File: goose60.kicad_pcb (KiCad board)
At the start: 2 copper layers, 285 x 94.6 mm, 190 parts, among them J1 Debugger, J2 USART, J3 SPI, P1 USB_C_Plug_USB2.0, SW1 SW_Push, SW10 SW_Push, SW11 SW_Push, SW14 SW_Push, SW15 SW_Push, SW16 SW_Push, SW18 SW_Push, SW2 SW_Push, SW20 SW_Push, SW21 SW_Push, SW22 SW_Push, SW23 SW_Push, SW24 SW_Push, SW25 SW_Push, SW26 SW_Push, SW27 SW_Push, SW28 SW_Push, SW29 SW_Push, SW3 SW_Push, SW30 SW_Push, SW31 SW_Push, SW32 SW_Push, SW35 SW_Push, SW36 SW_Push, SW37 SW_Push, SW38 SW_Push, SW39 SW_Push, SW40 SW_Push, SW41 SW_Push, SW42 SW_Push, SW43 SW_Push, SW44 SW_Push, SW45 SW_Push, SW46 SW_Push, SW47 SW_Push, SW48 SW_Push, SW49 SW_Push, SW5 SW_Push, SW50 SW_Push, SW51 SW_Push, SW52 SW_Push, SW53 SW_Push, SW54 SW_Push, SW56 SW_Push, SW58 SW_Push, SW59 SW_Push, SW60 SW_Push, SW61 SW_Push, SW62 SW_Push, SW65 SW_Push, SW66 SW_Push, SW67 SW_Push, SW68 SW_Push, SW69 SW_Push, SW7 SW_Push, SW71 SW_Push, SW73 SW_Push, SW74 SW_Push, SW75 SW_Push, SW76 SW_Push, SW78 SW_Push, SW79 SW_Push, SW80 SW_Push, SW82 SW_Push, SW84 SW_Push, SW86 SW_Push, SW9 SW_Push, U1 STM32F103CBTx, U2 LM317_SOT-223, X1 Crystal_GND24

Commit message: change pin default and try layout
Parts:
- removed ? (x4): , 
- removed HOLE: VAL**, hole:PKRH
- removed HOLE: VAL**, hole:PKRHSL
- removed P1: USB_C_Plug_USB2.0, Connector_USB:USB_C_Receptacle_HRO_TYPE-C-31-M-12
- removed R10, R9: 20, Resistor_SMD:R_0603_1608Metric
- removed R11: 1.5K, Resistor_SMD:R_0603_1608Metric
- added J4: USB_C_Receptacle_USB2.0, Connector_USB:USB_C_Receptacle_HRO_TYPE-C-31-M-12, B.Cu at (80.7, 66.5)
- added U3: USBLC6-2SC6, Package_TO_SOT_SMD:SOT-23-6, B.Cu at (94.0, 86.8)
- H2, H3, H5, H6: footprint MountingHole:MountingHole_3.2mm_M3_Pad -> MountingHole:MountingHole_3.2mm_M3_Pad_TopOnly
- H4: footprint MountingHole:MountingHole_3.2mm_M3 -> MountingHole:MountingHole_3.2mm_M3_Pad_TopOnly
- J2, J3: moved to B.Cu
- R25: value 0 -> 5.1K
- moved H1 170.5 mm to (87.7, 93.1)
- moved H4 115.1 mm to (253.0, 150.4)
- moved H3 106.1 mm to (322.6, 93.1)
- moved H2 90.6 mm to (190.7, 112.2)
- moved C9 38.5 mm to (131.0, 91.9)
- moved R5 38.5 mm to (129.1, 91.9)
- moved R6 38.5 mm to (127.2, 91.9)
- moved C10 38.3 mm to (140.0, 86.3)
- moved C11 38.2 mm to (124.7, 87.0)
- moved R4 38.2 mm to (125.3, 89.7)
- moved U2 38.2 mm to (133.1, 86.3)
- moved C8 38.2 mm to (126.9, 84.5)
- moved D69 38.2 mm to (124.8, 84.5)
- moved D70 38.2 mm to (127.3, 88.3)
- moved D6 20.8 mm to (82.5, 157.9), turned to 0 degrees
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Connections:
- J3 pad 2: SCK -> MOSI
- J3 pad 3: MOSI -> MISO
- J3 pad 4: MISO -> SCK
- R22 pad 2: PA8 -> PA4
- SW32 pad 2: col6 -> col7
- U1 pad 14: CAPS_LED -> PA4
- U1 pad 18: row2 -> col14
- U1 pad 20: col8 -> col13
- U1 pad 21: col9 -> col12
- U1 pad 22: col10 -> col11
- U1 pad 25: col11 -> col3
- U1 pad 26: col12 -> col2
- U1 pad 27: col13 -> col1
- U1 pad 28: col14 -> col4
- U1 pad 29: PA8 -> CAPS_LED
- U1 pad 39: col1 -> col5
- U1 pad 40: col2 -> col6
- U1 pad 41: col3 -> col7
- U1 pad 42: col4 -> col8
- U1 pad 43: col5 -> col9
- U1 pad 45: col6 -> row2
- U1 pad 46: col7 -> col10
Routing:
- net row2: track 0.00 -> 370.8 mm, vias 0 -> 16
- net row1: track 0.00 -> 304.4 mm, vias 0 -> 2
- net row4: track 0.00 -> 277.4 mm, vias 0 -> 13
- net row3: track 0.00 -> 269.3 mm, vias 0 -> 13
- net col13: track 0.00 -> 263.6 mm, vias 0 -> 3
- net row5: track 0.00 -> 259.0 mm
- net col10: track 0.00 -> 176.2 mm, vias 0 -> 2
- net col9: track 0.00 -> 160.0 mm, vias 0 -> 2
- net col1: track 0.00 -> 157.3 mm, vias 0 -> 2
- net col8: track 0.00 -> 142.6 mm, vias 0 -> 2
- net col7: track 0.00 -> 139.4 mm, vias 0 -> 2
- net col2: track 0.00 -> 137.9 mm, vias 0 -> 4
- net col14: track 0.00 -> 135.5 mm, vias 0 -> 3
- net col3: track 0.00 -> 118.9 mm, vias 0 -> 2
- net +3.3V: track 0.00 -> 117.1 mm
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
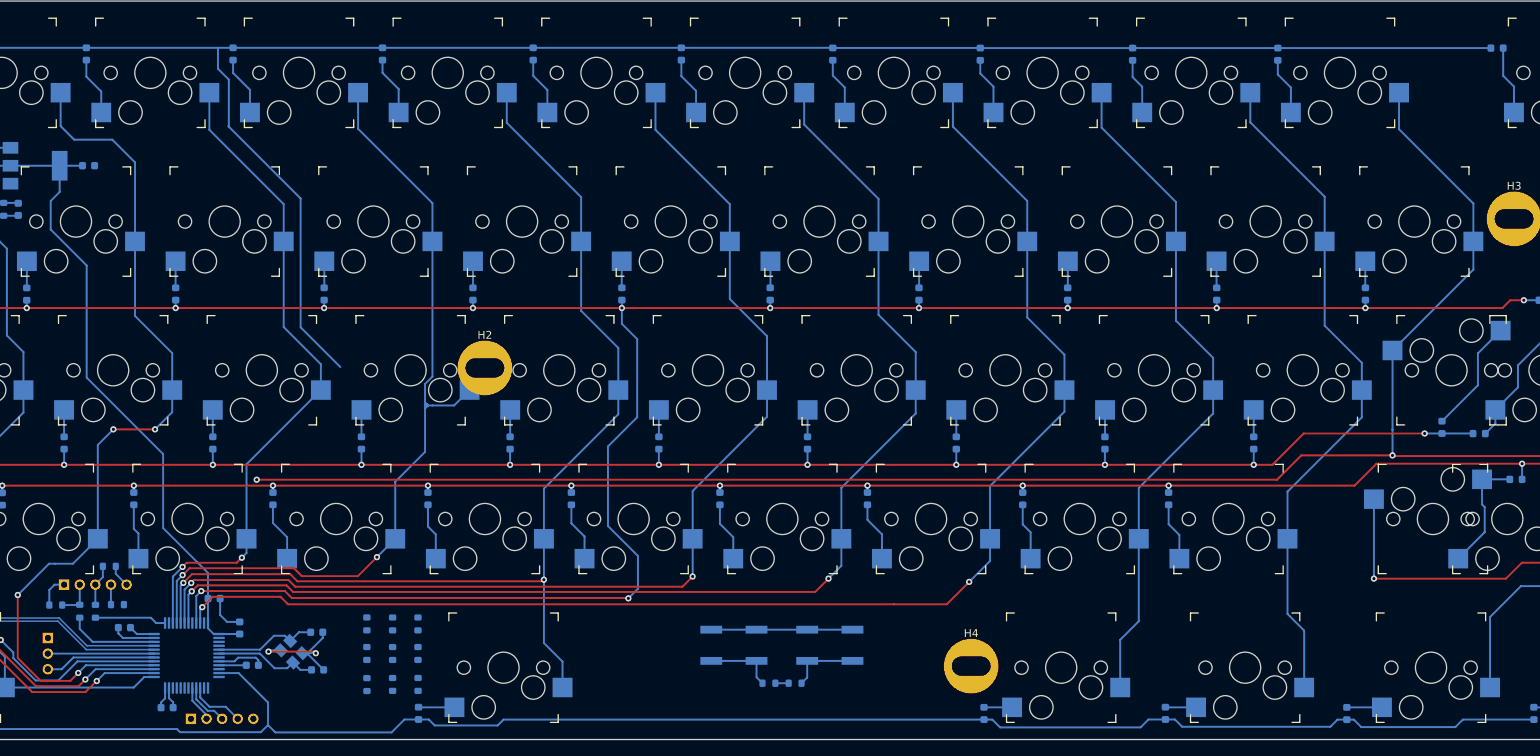
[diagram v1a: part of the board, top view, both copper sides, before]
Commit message: update pcb layout and pin defined
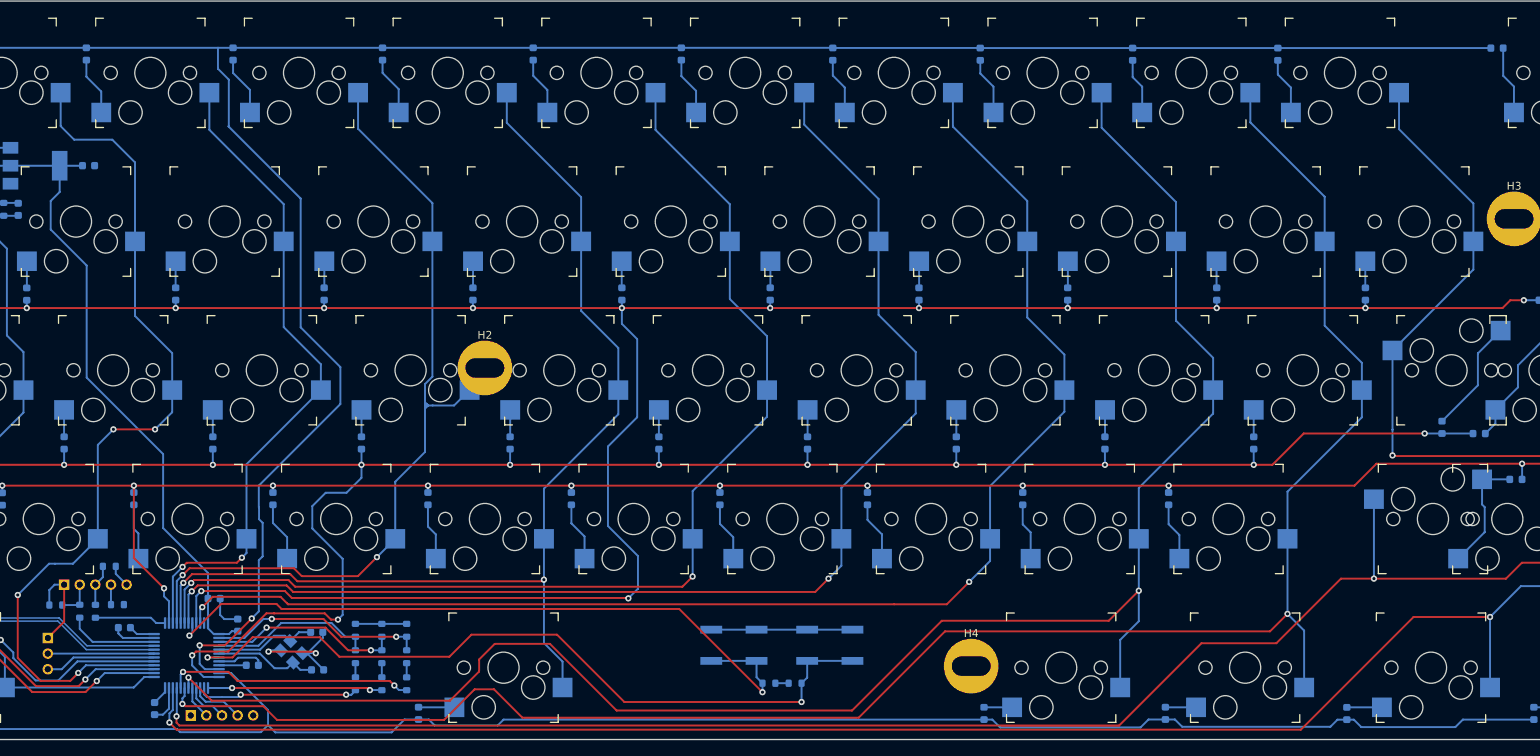
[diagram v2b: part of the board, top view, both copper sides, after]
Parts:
- moved R15 1.67 mm to (174.2, 145.8)
- moved R19 1.66 mm to (180.7, 145.8)
- moved C5 1.60 mm to (148.4, 155.8), turned to -90 degrees
- moved R17 1.60 mm to (177.5, 145.8)
- moved R16 1.52 mm to (174.2, 149.2)
- moved R20 1.51 mm to (180.7, 149.2)
- moved R23 1.47 mm to (174.2, 152.7)
- moved R21 1.46 mm to (180.7, 152.7)
- moved R18 1.44 mm to (177.5, 149.2)
- moved R22 1.38 mm to (177.5, 152.7)
- moved C3 0.44 mm to (159.1, 145.2)
- moved J3 0.43 mm to (153.1, 156.7)
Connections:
- R21 pad 2: PA0 -> PB2
- R22 pad 2: PA4 -> PA3
- R23 pad 2: PA15 -> PA4
- U1 pad 10: PA0 -> row1
- U1 pad 12: row4 -> row3
- U1 pad 13: row3 -> PA3
- U1 pad 18: col14 -> col11
- U1 pad 19: row1 -> col12
- U1 pad 20: col13 -> PB2
- U1 pad 21: col12 -> col14
- U1 pad 22: col11 -> col13
- U1 pad 38: PA15 -> row4
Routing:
- net col14: track 135.5 -> 301.4 mm, vias 3 -> 4
- net col12: track 86.9 -> 240.2 mm, vias 0 -> 2
- net col11: track 87.0 -> 225.2 mm, vias 0 -> 2
- net RESET: track 8.96 -> 95.8 mm, vias 0 -> 2
- net BOOT0: track 8.98 -> 91.7 mm, vias 0 -> 2
- net row3: track 269.3 -> 321.7 mm, vias 13 -> 15
- net row1: track 304.4 -> 355.0 mm, vias 2 -> 4
- net col13: track 263.6 -> 297.0 mm, vias 3 -> 4
- net PB2: track 0.00 -> 31.8 mm, vias 0 -> 2
- net PC13: track 0.00 -> 27.7 mm, vias 0 -> 2
- net PC14: track 0.00 -> 24.6 mm, vias 0 -> 2
- net PA3: track 0.00 -> 22.3 mm, vias 0 -> 2
- net PC15: track 0.00 -> 21.2 mm
- net PA4: track 0.00 -> 20.8 mm, vias 0 -> 2
- net row4: track 277.4 -> 296.9 mm, vias 13 -> 14
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
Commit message: add usb enable pin
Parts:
- removed R23: 10K, Resistor_SMD:R_0603_1608Metric
- added H7: MountingHole_Pad, NetTie:NetTie-2_SMD_Pad0.5mm, B.Cu at (82.1, 73.0)
- added H8: MountingHole_Pad, NetTie:NetTie-2_SMD_Pad0.5mm, B.Cu at (79.3, 73.0)
- added Q1: Q_NMOS_GSD, Package_TO_SOT_SMD:SOT-23, B.Cu at (110.0, 83.9)
- added R10: 22, Resistor_SMD:R_0603_1608Metric, B.Cu at (101.8, 85.9)
- added R11: 1.5K, Resistor_SMD:R_0603_1608Metric, B.Cu at (101.8, 83.9)
- added R26: 10K, Resistor_SMD:R_0603_1608Metric, B.Cu at (114.7, 84.8)
- added R9: 22, Resistor_SMD:R_0603_1608Metric, B.Cu at (101.8, 87.8)
- moved D22 1.40 mm to (130.3, 129.1)
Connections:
- J4 pad A8: unconnected-(J4-PadA8) -> Net-(J4-PadA8)
- J4 pad B8: unconnected-(J4-PadB8) -> Net-(J4-PadB8)
- U1 pad 14: PA4 -> USB_EN
- U3 pad 4: USB_D+ -> Net-(U3-Pad4)
- U3 pad 6: USB_D- -> Net-(U3-Pad6)
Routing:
- net USB_EN: track 0.00 -> 108.9 mm, vias 0 -> 4
- net +3.3V: track 123.3 -> 189.7 mm
- net PA4: track 20.8 -> 0.00 mm, vias 2 -> 0
- net VIN: track 67.6 -> 86.1 mm
- net Net-(U3-Pad4): track 0.00 -> 7.79 mm
- net Net-(R11-Pad2): track 0.00 -> 6.44 mm
- net Net-(U3-Pad6): track 0.00 -> 5.80 mm
- net col3: track 118.9 -> 113.8 mm, vias 2 -> 4
- net USB_D-: track 98.9 -> 94.0 mm
- net USB_D+: track 98.9 -> 93.9 mm
- net BOOT0: track 91.7 -> 88.7 mm
- net Net-(R26-Pad1): track 0.00 -> 2.95 mm
- net Net-(C9-Pad1): track 7.97 -> 10.8 mm
- net Net-(J4-PadB8): track 0.00 -> 2.28 mm
- net col4: track 113.8 -> 116.0 mm
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
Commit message: add gh60  mechanism hole
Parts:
- moved H5 163.0 mm to (64.0, 121.7)
- moved H6 149.2 mm to (346.1, 121.7)
- moved D59 6.85 mm to (337.1, 123.1)
- moved C4 0.75 mm to (160.6, 151.0)
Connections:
- R21 pad 2: PB2 -> PA4
- R22 pad 2: PA3 -> PA1
- U1 pad 11: row5 -> PA1
- U1 pad 13: PA3 -> row5
- U1 pad 14: USB_EN -> PA4
- U1 pad 20: PB2 -> USB_EN
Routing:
- net GND: track 123.8 -> 429.2 mm, vias 3 -> 18
- net +3.3V: track 189.7 -> 318.5 mm, vias 0 -> 3
- net PB2: track 32.2 -> 0.00 mm, vias 2 -> 0
- net PA4: track 0.00 -> 29.9 mm, vias 0 -> 2
- net PA3: track 22.8 -> 0.00 mm, vias 2 -> 0
- net PA1: track 0.00 -> 21.7 mm, vias 0 -> 2
- net RESET: track 97.6 -> 111.9 mm, vias 2 -> 3
- net Net-(D59-Pad1): track 3.72 -> 13.2 mm
- net row4: track 297.0 -> 290.0 mm
- net USB_EN: track 108.9 -> 102.7 mm
- net col4: track 116.0 -> 112.3 mm
- net col5: track 85.5 -> 88.4 mm
- net PC14: track 24.6 -> 27.1 mm
- net BOOT0: track 88.7 -> 91.2 mm
- net col6: track 106.8 -> 109.2 mm
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
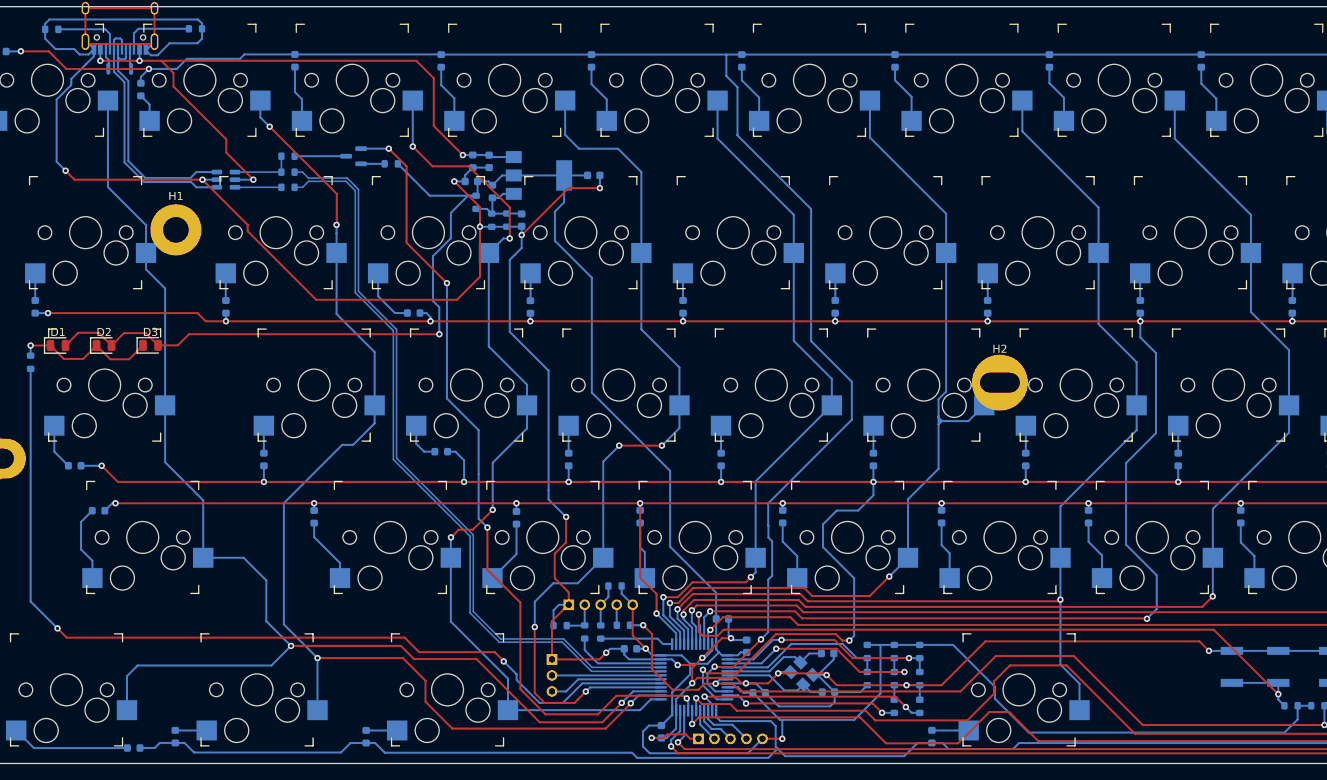
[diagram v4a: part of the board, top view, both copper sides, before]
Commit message: update MCU VCC and GND layout
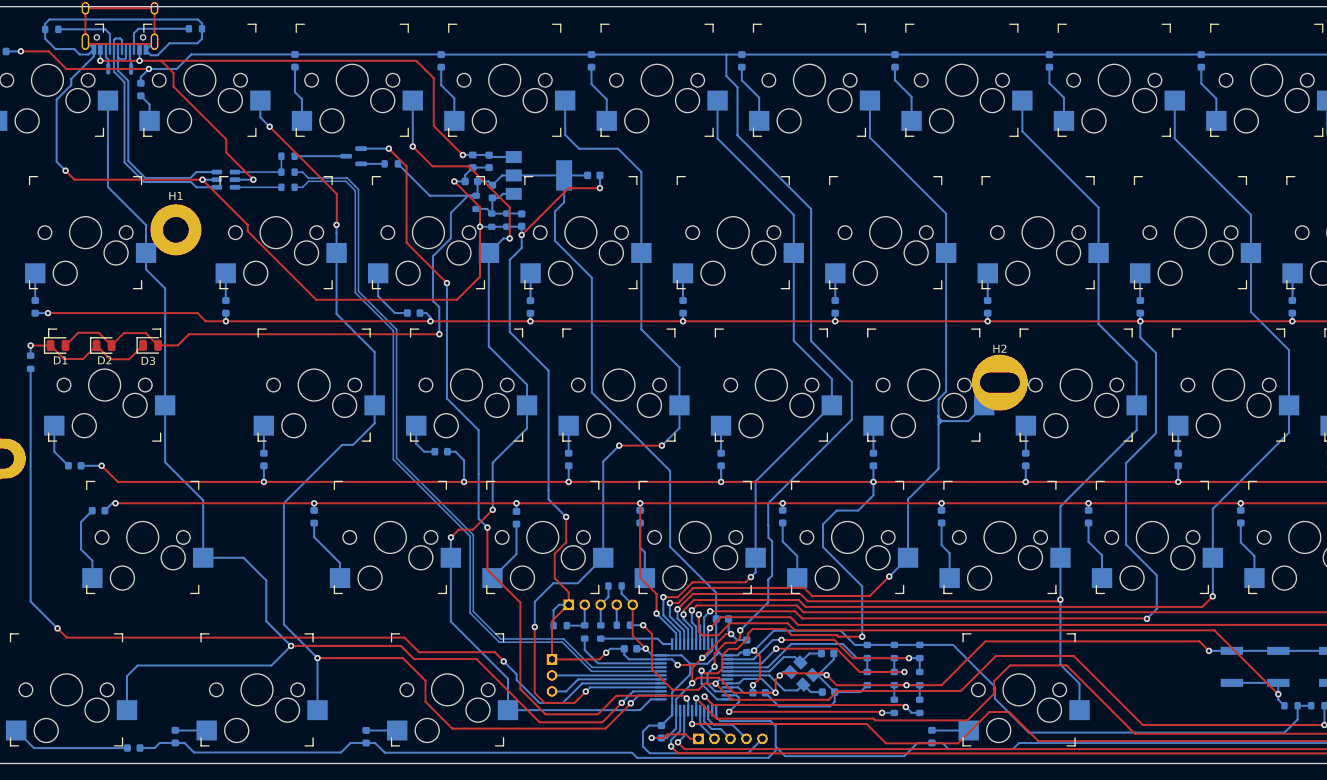
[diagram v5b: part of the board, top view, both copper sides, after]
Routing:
- net +3.3V: track 318.5 -> 311.7 mm, vias 3 -> 4
- net GND: track 429.2 -> 434.0 mm
- net row3: track 321.7 -> 324.8 mm
- net PA1: track 21.7 -> 24.5 mm
- net RESET: track 111.9 -> 112.8 mm
- net row1: track 354.4 -> 353.6 mm
- net col12: track 240.2 -> 239.5 mm
- net BOOT0: track 91.2 -> 91.8 mm
